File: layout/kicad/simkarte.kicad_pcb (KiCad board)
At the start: 2 copper layers, 101.5 x 54 mm, 14 parts, among them J1 SIM_Card, U1 ATtiny85-20PU, U2 ATtiny85-20PU

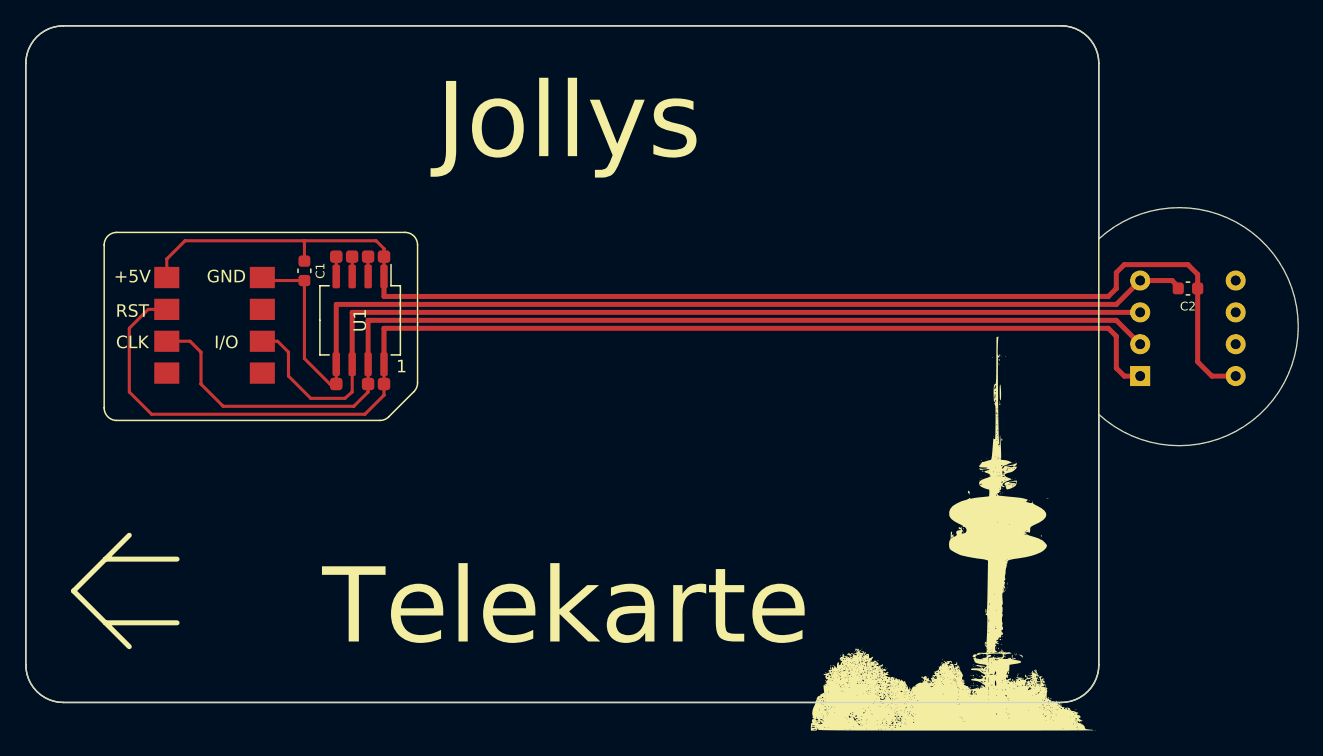
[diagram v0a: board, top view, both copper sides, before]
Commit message: C-Netz: Updated sim card layout to support memory card emulation.
A jumper must be switched in order to emulate the reset input.

Also added new service codes to the silk mask.
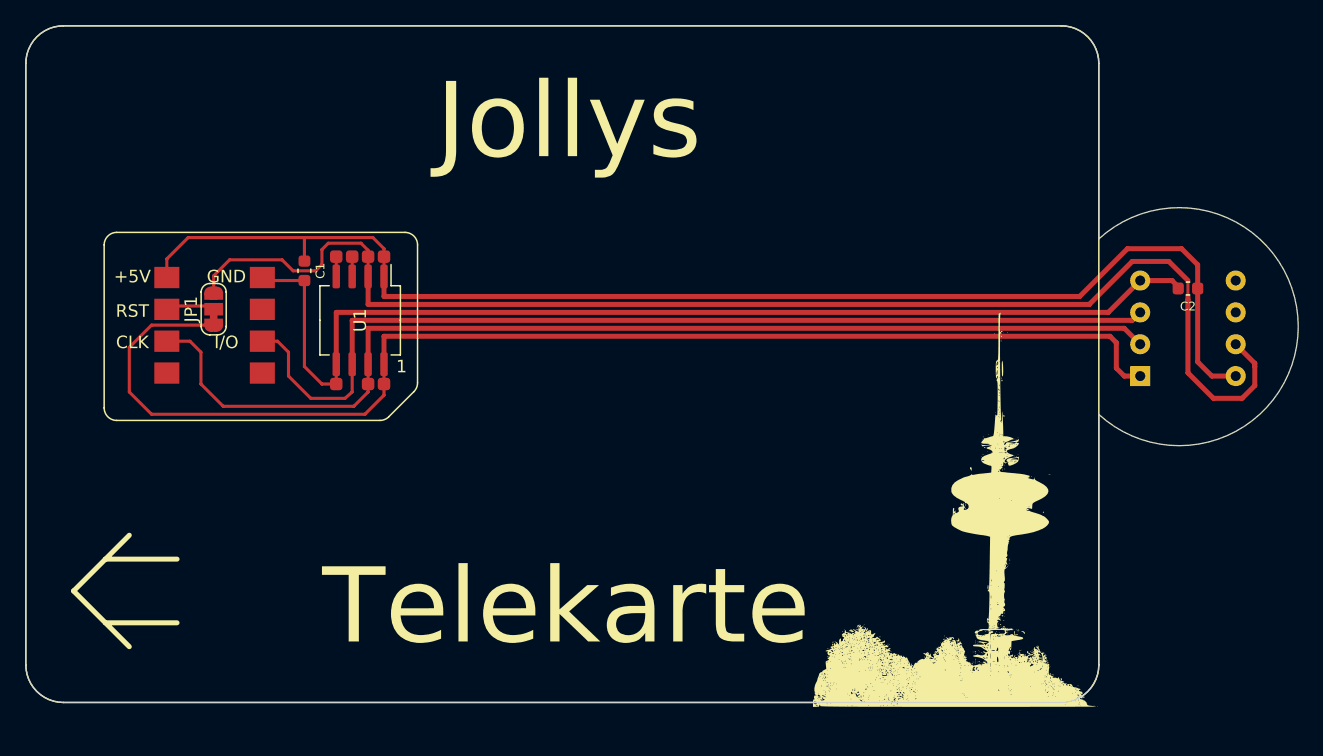
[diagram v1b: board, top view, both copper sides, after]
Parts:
- added JP1: Jumper_3_Bridged12, Jumper:SolderJumper-3_P1.3mm_Bridged12_RoundedPad1.0x1.5mm_NumberLabels, F.Cu at (121.7, 96.3)
- moved G*** 1.90 mm to (184.5, 111.3)
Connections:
- TP7 pad 1: Net-(J1-Pad2) -> Net-(TP7-Pad1)
- U1 pad 1: Net-(J1-Pad2) -> Net-(TP7-Pad1)
- U2 pad 1: Net-(J1-Pad2) -> Net-(TP7-Pad1)
- U2 pad 7: unconnected-(U2-Pad7) -> Net-(TP5-Pad1)
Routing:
- net Net-(TP5-Pad1): track 2.00 -> 106.5 mm
- net Net-(TP7-Pad1): track 0.00 -> 100.3 mm
- net Net-(J1-Pad2): track 99.1 -> 3.95 mm
- net +5V: track 102.6 -> 103.8 mm
- net Net-(J1-Pad3): track 88.3 -> 87.4 mm
